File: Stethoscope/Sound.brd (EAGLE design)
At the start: 70 x 70 mm, 24 parts

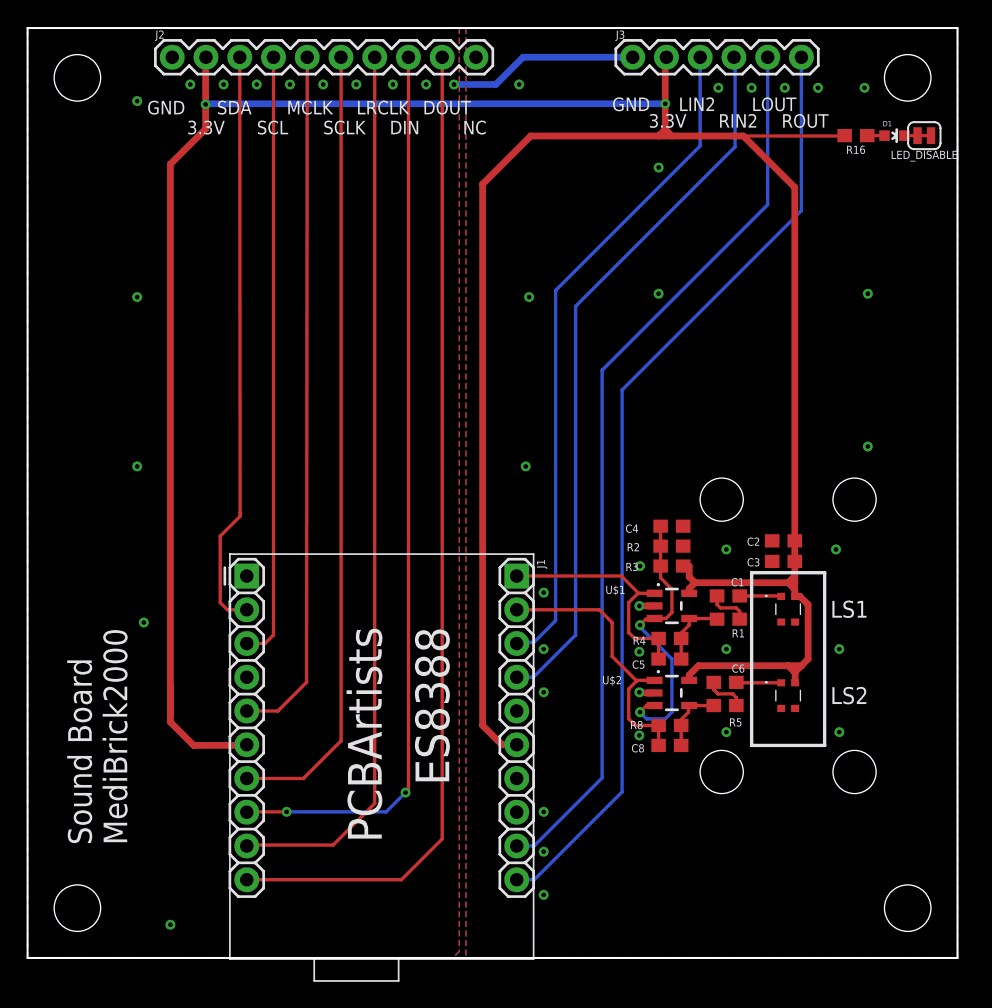
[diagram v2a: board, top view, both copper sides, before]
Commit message: Board Updates
Separated analog and digital ground
Updated routing
Updated silk labeling
Sound board with ES8388 included
Impedance and ECG board
Working on IMU board
Working on Environmental Airquality board
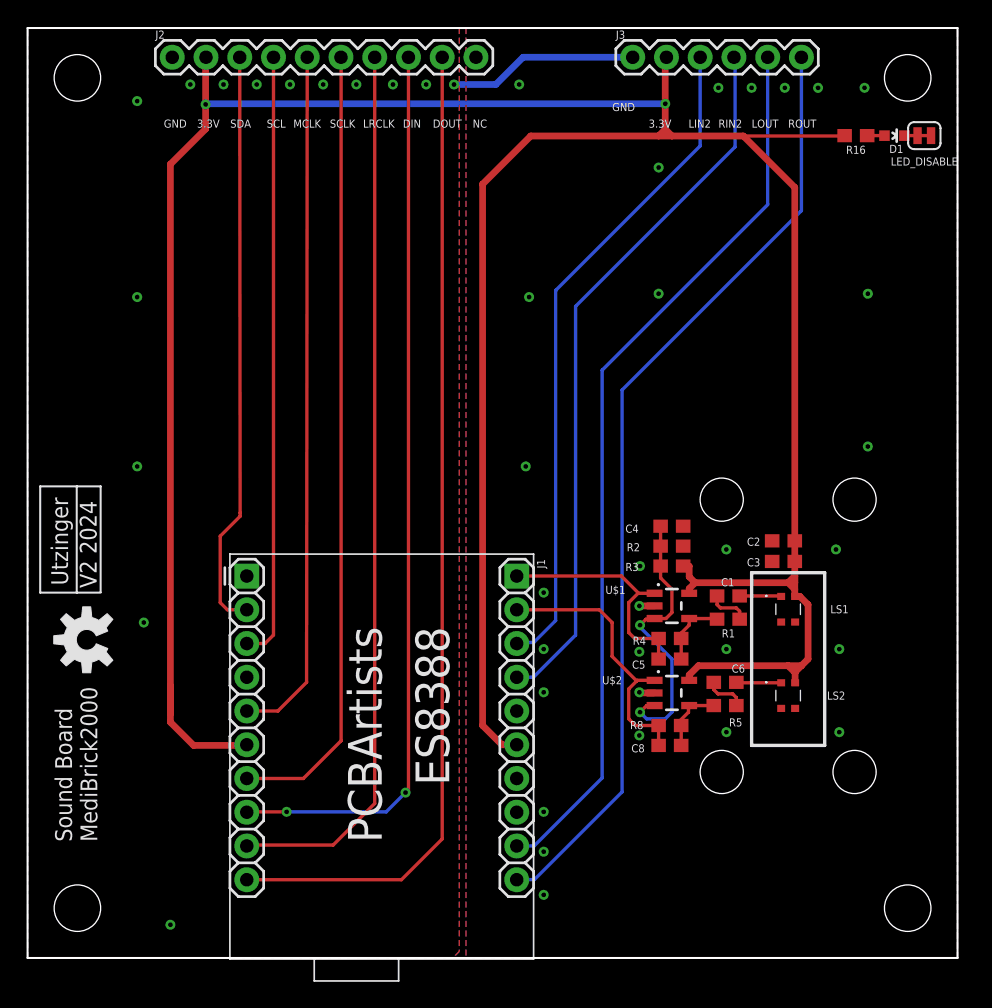
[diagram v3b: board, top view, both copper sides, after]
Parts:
- added U$3: (no value), SparkFun-Aesthetics:OSHW-LOGO-M
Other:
- board text added: "Utzinger"
- board text added: "V2 2024"
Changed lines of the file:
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@@
 <hole x="66.25" y="3.75" drill="3.5"/>
 <hole x="3.75" y="3.75" drill="3.5"/>
-<text x="7.5" y="8.5" size="1.778" layer="25" rot="R90">Sound Board
+<text x="5.25" y="8.75" size="1.27" layer="25" rot="R90">Sound Board
 MediBrick2000</text>
 <wire x1="0" y1="0" x2="0" y2="70" width="0.1524" layer="20"/>
@@
 <wire x1="70" y1="0" x2="0" y2="0" width="0.1524" layer="20"/>
 <dimension x1="0" y1="0" x2="24.8" y2="0" x3="12.4" y3="-3" textsize="1.778" layer="1"/>
-<text x="12" y="62" size="1.016" layer="25">3.3V</text>
-<text x="9" y="63.5" size="1.016" layer="25">GND</text>
-<text x="14.25" y="63.5" size="1.016" layer="25">SDA</text>
-<text x="17.25" y="62" size="1.016" layer="25">SCL</text>
-<text x="22.25" y="62" size="1.016" layer="25">SCLK</text>
-<text x="27.25" y="62" size="1.016" layer="25">DIN</text>
-<text x="19.5" y="63.5" size="1.016" layer="25">MCLK</text>
-<text x="24.75" y="63.5" size="1.016" layer="25">LRCLK</text>
-<text x="29.75" y="63.5" size="1.016" layer="25">DOUT</text>
-<text x="44" y="63.75" size="1.016" layer="25">GND</text>
-<text x="46.75" y="62.5" size="1.016" layer="25">3.3V</text>
-<text x="49" y="63.75" size="1.016" layer="25">LIN2</text>
-<text x="52" y="62.5" size="1.016" layer="25">RIN2</text>
-<text x="54.5" y="63.75" size="1.016" layer="25">LOUT</text>
-<text x="56.75" y="62.5" size="1.016" layer="25">ROUT</text>
+<text x="12.75" y="62.5" size="0.6096" layer="25" font="vector" ratio="20">3.3V</text>
+<text x="10.25" y="62.5" size="0.6096" layer="25" font="vector" ratio="20">GND</text>
+<text x="15.25" y="62.5" size="0.6096" layer="25" font="vector" ratio="20">SDA</text>
+<text x="18" y="62.5" size="0.6096" layer="25" font="vector" ratio="20">SCL</text>
+<text x="22.75" y="62.5" size="0.6096" layer="25" font="vector" ratio="20">SCLK</text>
+<text x="28.25" y="62.5" size="0.6096" layer="25" font="vector" ratio="20">DIN</text>
+<text x="20" y="62.5" size="0.6096" layer="25" font="vector" ratio="20">MCLK</text>
+<text x="25.25" y="62.5" size="0.6096" layer="25" font="vector" ratio="20">LRCLK</text>
+<text x="30.5" y="62.5" size="0.6096" layer="25" font="vector" ratio="20">DOUT</text>
+<text x="44" y="63.75" size="0.6096" layer="25" font="vector" ratio="20">GND</text>
+<text x="46.75" y="62.5" size="0.6096" layer="25" font="vector" ratio="20">3.3V</text>
+<text x="49.75" y="62.5" size="0.6096" layer="25" font="vector" ratio="20">LIN2</text>
+<text x="52" y="62.5" size="0.6096" layer="25" font="vector" ratio="20">RIN2</text>
+<text x="54.5" y="62.5" size="0.6096" layer="25" font="vector" ratio="20">LOUT</text>
+<text x="57.25" y="62.5" size="0.6096" layer="25" font="vector" ratio="20">ROUT</text>
 <hole x="52.25" y="14" drill="3.25"/>
 <hole x="62.25" y="14" drill="3.25"/>
@@
 <wire x1="54.5" y1="16" x2="54.5" y2="29" width="0.254" layer="25"/>
 <dimension x1="0" y1="-4" x2="57.25" y2="-4" x3="28.625" y3="-7" textsize="1.778" layer="1"/>
-<text x="32.75" y="62" size="1.016" layer="25">NC</text>
+<text x="33.5" y="62.5" size="0.6096" layer="25" font="vector" ratio="20">NC</text>
+<text x="3.05" y="28.05" size="1.27" layer="25" font="vector" rot="R90">Utzinger</text>
+<wire x1="0.95" y1="27.5" x2="0.95" y2="35.5" width="0.1524" layer="25"/>
+<wire x1="0.95" y1="35.5" x2="3.7" y2="35.5" width="0.1524" layer="25"/>
+<wire x1="3.7" y1="35.5" x2="3.7" y2="27.5" width="0.1524" layer="25"/>
+<wire x1="3.7" y1="27.5" x2="0.95" y2="27.5" width="0.1524" layer="25"/>
+<wire x1="5.5" y1="27.55" x2="5.5" y2="35.5" width="0.1524" layer="25"/>
+<wire x1="5.5" y1="27.5" x2="3.7" y2="27.5" width="0.1524" layer="25"/>
+<wire x1="5.5" y1="35.5" x2="3.7" y2="35.5" width="0.1524" layer="25"/>
+<text x="5.2" y="27.85" size="1.27" layer="25" font="vector" ratio="20" rot="R90">V2 2024</text>
 </plain>
 <attributes>
@@
 </element>
 <element name="D1" library="SparkFun-LED" package="LED-0603" value="RED" x="65.25" y="61.9" smashed="yes" rot="R270">
-<attribute name="NAME" x="64.361" y="62.5985" size="0.4064" layer="25"/>
+<attribute name="NAME" x="64.861" y="60.5985" size="0.6096" layer="25" font="vector" ratio="20"/>
 <attribute name="PROD_ID" value="DIO-00819" x="72.25" y="64.9" size="1.778" layer="27" rot="R270" display="off"/>
-<attribute name="VALUE" x="64.234" y="60.8205" size="0.4064" layer="27"/>
+<attribute name="VALUE" x="64.234" y="60.8205" size="0.4064" layer="27" display="off"/>
 </element>
 <element name="LED_DISABLE" library="SparkFun-Jumpers" library_urn="urn:adsk.eagle:library:528" package="SMT-JUMPER_2_NC_TRACE_SILK" package3d_urn="urn:adsk.eagle:package:39281/1" value="JUMPER-SMT_2_NC_TRACE_SILK" x="67.5" y="61.9" smashed="yes" rot="R180">
-<attribute name="NAME" x="67.5" y="60.757" size="0.6096" layer="25" font="vector" ratio="20" rot="R180" align="bottom-center"/>
+<attribute name="NAME" x="67.5" y="60.257" size="0.6096" layer="25" font="vector" ratio="20" rot="R180" align="bottom-center"/>
 <attribute name="VALUE" x="67.5" y="63.043" size="0.6096" layer="27" font="vector" ratio="20" rot="R180" align="top-center" display="off"/>
 </element>
@@
 <attribute name="MOUSER_PART_NUMBER" value="665-AMM-2742-T-R" x="57.25" y="26.25" size="1.778" layer="27" display="off"/>
 <attribute name="MOUSER_PRICE-STOCK" value="https://www.mouser.co.uk/ProductDetail/PUI-Audio/AMM-2742-T-R?qs=zhx2xqPtQQyJoGop0O%252BpMA%3D%3D" x="57.25" y="26.25" size="1.778" layer="27" display="off"/>
-<attribute name="NAME" x="61.862" y="26.25" size="1.27" layer="25" align="center"/>
-<attribute name="VALUE" x="60.862" y="23" size="1.27" layer="27" align="center"/>
+<attribute name="NAME" x="61.112" y="26.25" size="0.6096" layer="25" font="vector" ratio="20" align="center"/>
+<attribute name="VALUE" x="60.862" y="23" size="0.6096" layer="27" font="vector" align="center"/>
 </element>
 <element name="C2" library="SparkFun-Capacitors" library_urn="urn:adsk.eagle:library:510" package="0603" package3d_urn="urn:adsk.eagle:package:37414/1" value="10uF" x="56.9" y="31.4" smashed="yes" rot="R180">
@@
 </element>
 <element name="C1" library="SparkFun-Capacitors" library_urn="urn:adsk.eagle:library:510" package="0603" package3d_urn="urn:adsk.eagle:package:37414/1" value="4.7uF" x="52.75" y="27.25" smashed="yes" rot="R180">
-<attribute name="NAME" x="53.45" y="28.588" size="0.6096" layer="25" font="vector" ratio="20" rot="R180" align="bottom-center"/>
+<attribute name="NAME" x="52.7" y="28.588" size="0.6096" layer="25" font="vector" ratio="20" rot="R180" align="bottom-center"/>
 <attribute name="PROD_ID" value="CAP-08280" x="52.75" y="27.25" size="1.778" layer="27" rot="R180" display="off"/>
-<attribute name="VALUE" x="51.55" y="28.012" size="0.6096" layer="27" font="vector" ratio="20" rot="R180" align="top-center"/>
+<attribute name="VALUE" x="52.8" y="29.012" size="0.6096" layer="27" font="vector" ratio="20" rot="R180" align="top-center"/>
 </element>
 <element name="R1" library="SparkFun-Resistors" library_urn="urn:adsk.eagle:library:532" package="0603" package3d_urn="urn:adsk.eagle:package:39650/1" value="4.7k" x="52.75" y="25.5" smashed="yes" rot="R180">
-<attribute name="NAME" x="53.5" y="24.738" size="0.6096" layer="25" font="vector" ratio="20" rot="R180" align="bottom-center"/>
+<attribute name="NAME" x="52.75" y="24.738" size="0.6096" layer="25" font="vector" ratio="20" rot="R180" align="bottom-center"/>
 <attribute name="PROD_ID" value="RES-07857" x="52.75" y="25.5" size="1.778" layer="27" rot="R180" display="off"/>
-<attribute name="VALUE" x="51.85" y="24.162" size="0.6096" layer="27" font="vector" ratio="20" rot="R180" align="top-center"/>
+<attribute name="VALUE" x="51.1" y="24.162" size="0.6096" layer="27" font="vector" ratio="20" rot="R180" align="top-center"/>
 </element>
 <element name="R2" library="SparkFun-Resistors" library_urn="urn:adsk.eagle:library:532" package="0603" package3d_urn="urn:adsk.eagle:package:39650/1" value="10k" x="48.5" y="29.5" smashed="yes">
@@
 <attribute name="MOUSER_PART_NUMBER" value="665-AMM-2742-T-R" x="54.25" y="19.75" size="1.778" layer="27" display="off"/>
 <attribute name="MOUSER_PRICE-STOCK" value="https://www.mouser.co.uk/ProductDetail/PUI-Audio/AMM-2742-T-R?qs=zhx2xqPtQQyJoGop0O%252BpMA%3D%3D" x="54.25" y="19.75" size="1.778" layer="27" display="off"/>
-<attribute name="NAME" x="61.862" y="19.75" size="1.27" layer="25" align="center"/>
-<attribute name="VALUE" x="60.862" y="17.25" size="1.27" layer="27" align="center"/>
+<attribute name="NAME" x="60.862" y="19.75" size="0.6096" layer="25" font="vector" ratio="20" align="center"/>
+<attribute name="VALUE" x="60.862" y="17.25" size="0.6096" layer="27" font="vector" align="center"/>
 </element>
 <element name="U$2" library="SparkFun-IC-Amplifiers" library_urn="urn:adsk.eagle:library:520" package="SOT23-5" package3d_urn="urn:adsk.eagle:package:38670/1" value="OPA344" x="48.5" y="19.95" smashed="yes" rot="R270">
@@
 <attribute name="VALUE" x="44.1" y="17.212" size="0.6096" layer="27" font="vector" ratio="20" rot="R180" align="top-center"/>
 </element>
+<element name="U$3" library="SparkFun-Aesthetics" library_urn="urn:adsk.eagle:library:507" package="OSHW-LOGO-M" package3d_urn="urn:adsk.eagle:package:37126/1" value="" x="4.45" y="23.95" smashed="yes" rot="R90"/>
 </elements>
 <signals>
